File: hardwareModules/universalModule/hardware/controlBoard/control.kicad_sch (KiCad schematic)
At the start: 43 parts, among them J1 DEBUG, J22 SHOE_OUT, J5 SHOE_B1, J6 SHOE_B2, J8 USB_C_Receptacle_USB2.0, U11 STM32F411CEUx, U12 HT7533-1-SOT89, U6 ESP32-WROVER, U7 MPU-6050, Y1 7D024000H01

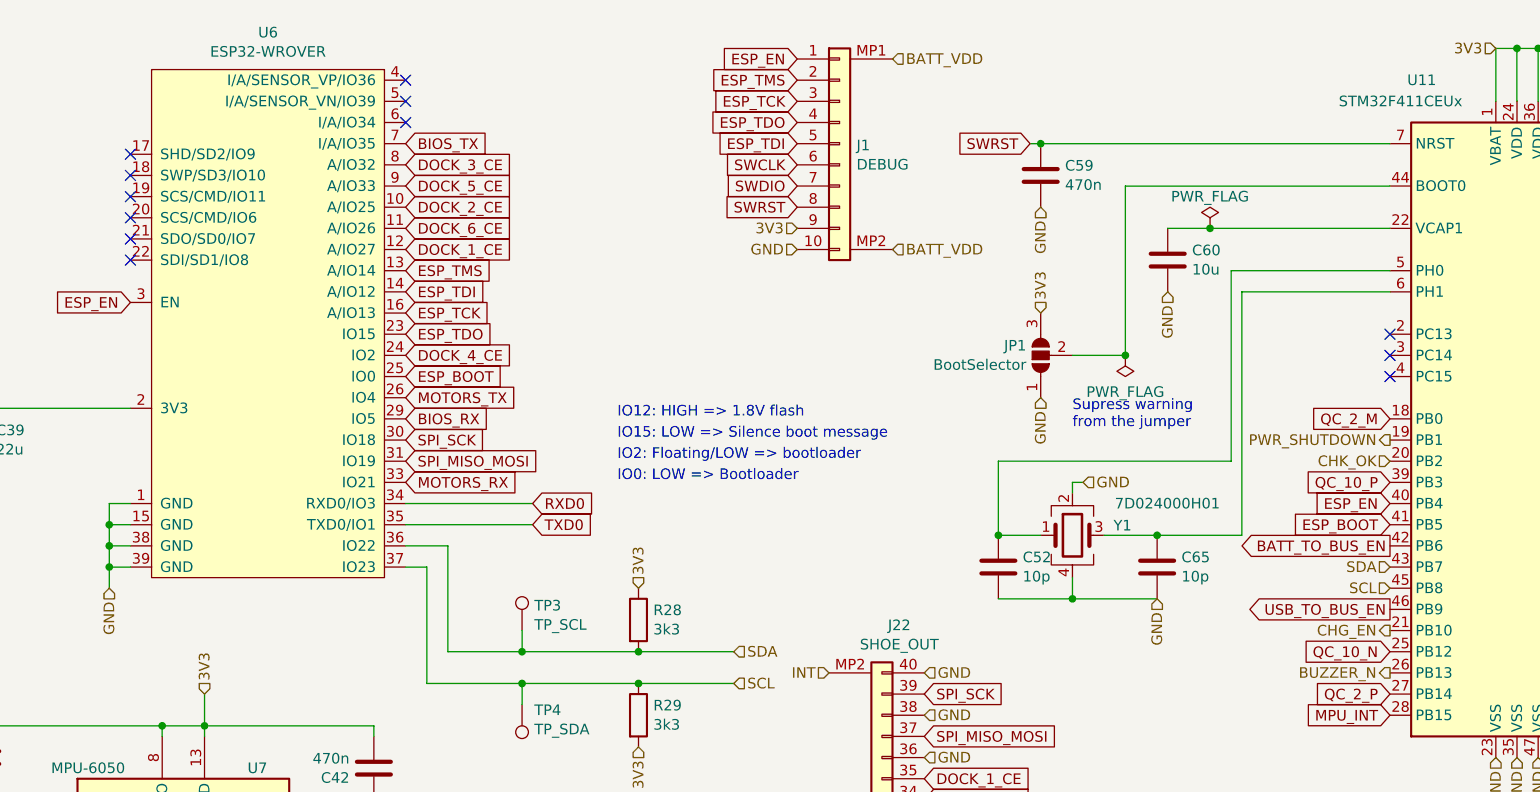
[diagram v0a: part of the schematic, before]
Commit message: um: Fix hardware bugs, prepare v0.5
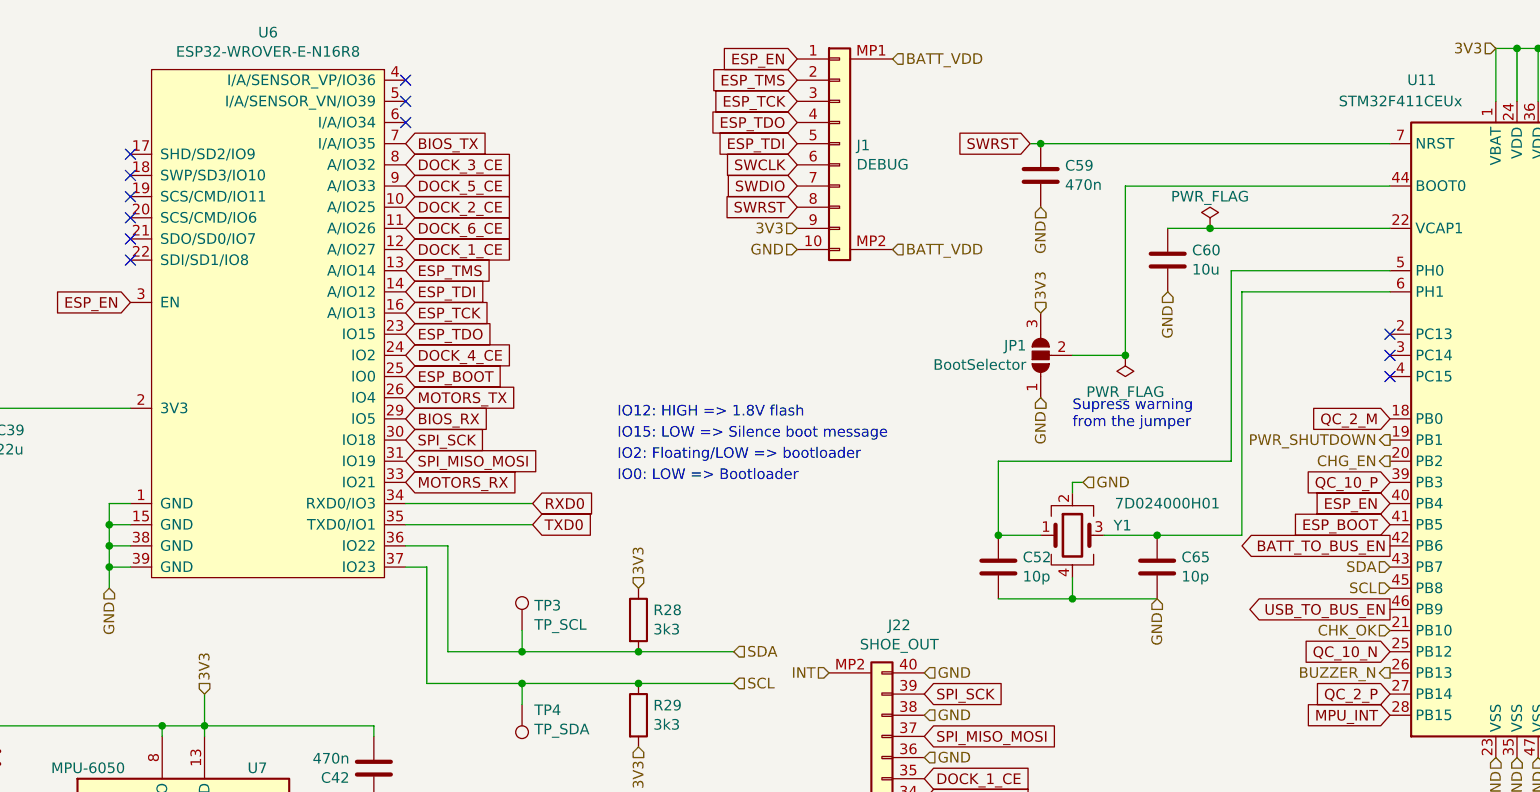
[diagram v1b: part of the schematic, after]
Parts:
- J6: MFR 120220-0161 -> 120220-0204
- J8: JLCPCB_CORRECTION 1.8;-3.3;180 -> 0;3.3;0
- U11: JLCPCB_CORRECTION 0;0;90 -> 0;0;-90
- U6: value ESP32-WROVER -> ESP32-WROVER-E-N16R8; LCSC C529591 -> C529589
- Y1: JLCPCB_CORRECTION (none) -> 0;0;180
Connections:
- net CHG_EN: now also U11.20 (PB2); no longer U11.21 (PB10)
- net CHK_OK: now also U11.21 (PB10); no longer U11.20 (PB2)
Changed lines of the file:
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@@
     (effects (font (size 1.27 1.27)) (justify left))
   )
-  (hierarchical_label "CHG_EN" (shape output) (at 190.5 87.63 180)
+  (hierarchical_label "CHG_EN" (shape output) (at 190.5 67.31 180)
     (effects (font (size 1.27 1.27)) (justify right))
   )
@@
     (effects (font (size 1.27 1.27)) (justify left))
   )
-  (hierarchical_label "CHK_OK" (shape input) (at 190.5 67.31 180)
+  (hierarchical_label "CHK_OK" (shape input) (at 190.5 87.63 180)
     (effects (font (size 1.27 1.27)) (justify right))
   )
@@
     (in_bom yes) (on_board yes)
     (property "Reference" "U6" (id 0) (at 55.88 15.875 0))
-    (property "Value" "ESP32-WROVER" (id 1) (at 55.88 18.1864 0))
+    (property "Value" "ESP32-WROVER-E-N16R8" (id 1) (at 55.88 18.1864 0))
     (property "Footprint" "rofi:ESP32-WROVER" (id 2) (at 55.88 26.67 0)
       (effects (font (size 1.27 1.27)) hide)
@@
       (effects (font (size 1.27 1.27)) hide)
     )
-    (property "LCSC" "C529591" (id 5) (at 55.88 50.8 0)
+    (property "LCSC" "C529589" (id 5) (at 55.88 50.8 0)
       (effects (font (size 1.27 1.27)) hide)
     )
@@
       (effects (font (size 1.27 1.27)) hide)
     )
-    (property "JLCPCB_CORRECTION" "1.8;-3.3;180" (id 5) (at 180.34 132.08 0)
+    (property "JLCPCB_CORRECTION" "0;3.3;0" (id 5) (at 180.34 132.08 0)
       (effects (font (size 1.27 1.27)) hide)
     )
@@
       (effects (font (size 1.27 1.27)) hide)
     )
-    (property "JLCPCB_CORRECTION" "0;0;90" (id 5) (at 208.28 62.23 0)
+    (property "JLCPCB_CORRECTION" "0;0;-90" (id 5) (at 208.28 62.23 0)
       (effects (font (size 1.27 1.27)) hide)
     )
@@
       (effects (font (size 1.27 1.27)) hide)
     )
-    (property "MFR" "120220-0161" (id 4) (at 41.91 170.18 0)
+    (property "MFR" "120220-0204" (id 4) (at 41.91 170.18 0)
       (effects (font (size 1.27 1.27)) hide)
     )
@@
       (effects (font (size 1.27 1.27)) hide)
     )
+    (property "JLCPCB_CORRECTION" "0;0;180" (id 5) (at 152.4 76.2 0)
+      (effects (font (size 1.27 1.27)) hide)
+    )

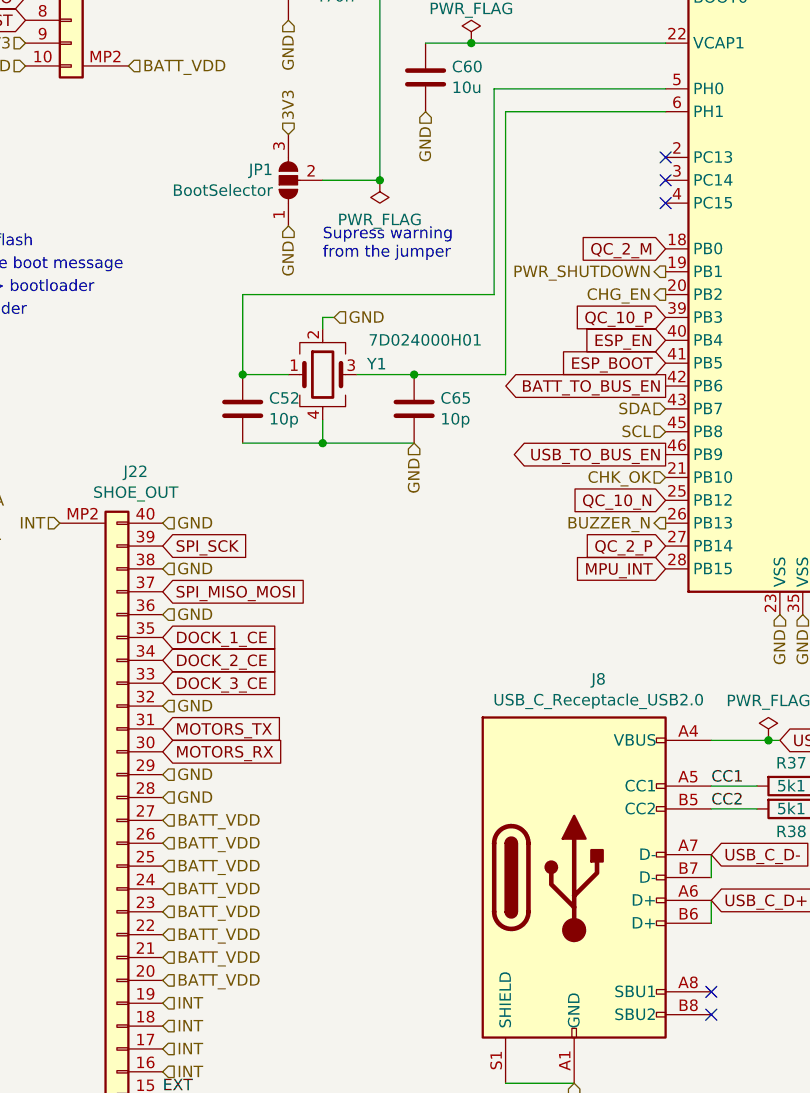
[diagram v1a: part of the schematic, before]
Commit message: hardware: Add custom FPC cables
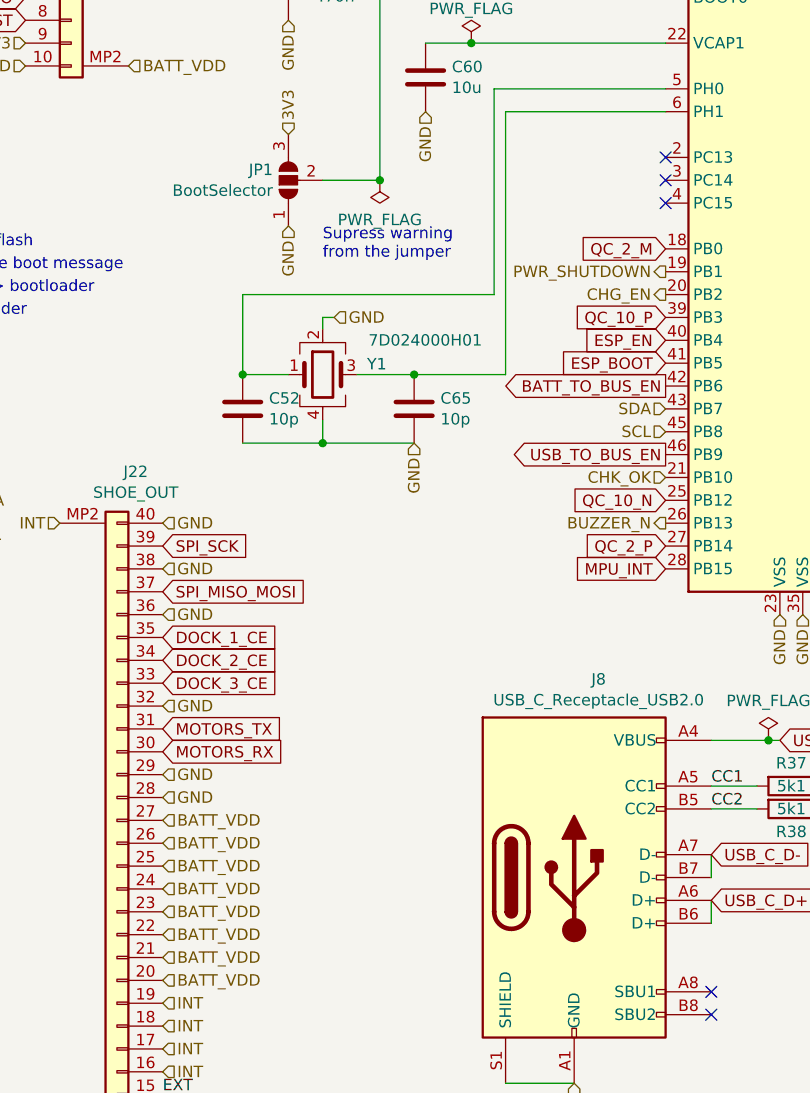
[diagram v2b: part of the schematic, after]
